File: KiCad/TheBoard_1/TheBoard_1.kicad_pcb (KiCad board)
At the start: 2 copper layers, 27 parts, among them J1 Conn_01x16_Female, J2 Conn_01x16_Female, U1 TL431D, U2 TL431D, U3 YAAJ_BlackPill_Part_Like_SWD_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, U4 TL431D, U5 TL431D

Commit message: progress
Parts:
- added J3: Conn_01x01_Male, Connector_PinHeader_2.54mm:PinHeader_1x01_P2.54mm_Vertical, F.Cu at (188.8, 80.0)
- added J4: Conn_01x01_Male, Connector_PinHeader_2.54mm:PinHeader_1x01_P2.54mm_Vertical, F.Cu at (188.2, 125.5)
- added J5: Conn_01x01_Male, Connector_PinHeader_2.54mm:PinHeader_1x01_P2.54mm_Vertical, F.Cu at (94.2, 145.8)
- added J6: Conn_01x01_Male, Connector_PinHeader_2.54mm:PinHeader_1x01_P2.54mm_Vertical, F.Cu at (102.0, 108.5)
- U3: value YAAJ_BlackPill_Part_Like_SWD_Breakout -> YAAJ_WeAct_BlackPill_Part_Like_SWD_Breakout
- moved U5 28.5 mm to (190.0, 97.4)
- moved Cref4 28.3 mm to (178.7, 144.5), turned to -90 degrees
- moved R3 28.0 mm to (182.3, 91.5)
- moved Cref3 26.6 mm to (180.2, 95.6), turned to -90 degrees
- moved R4 23.3 mm to (180.8, 139.0)
- moved U4 17.9 mm to (188.2, 146.3)
- moved R_SDA3 15.0 mm to (193.8, 66.3), turned to 180 degrees
- moved R_SCL3 13.3 mm to (193.8, 61.5), turned to 180 degrees
- moved R_SCL4 13.1 mm to (193.5, 107.3), turned to 180 degrees
- moved Udac4 10.5 mm to (188.2, 119.3)
- moved R_SDA4 9.63 mm to (193.5, 111.8), turned to 180 degrees
- moved Udac3 9.59 mm to (188.8, 73.3)
- moved U3 6.02 mm to (149.8, 81.2)
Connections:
- U3 pad 1: unconnected-(U3-Pad1) -> Net-(U3-Pad1)
- U3 pad 10: unconnected-(U3-Pad10) -> Net-(U3-Pad10)
- U3 pad 11: unconnected-(U3-Pad11) -> Net-(R_SCL2-Pad2)
- U3 pad 13: unconnected-(U3-Pad13) -> Net-(R_SDA2-Pad2)
- U3 pad 17: unconnected-(U3-Pad17) -> Net-(U3-Pad17)
- U3 pad 2: unconnected-(U3-Pad2) -> Net-(R_SCL1-Pad2)
- U3 pad 27: unconnected-(U3-Pad27) -> Net-(R_SDA1-Pad2)
- U3 pad 30: unconnected-(U3-Pad30) -> Net-(U3-Pad30)
- U3 pad 31: unconnected-(U3-Pad31) -> Net-(R_SCL4-Pad2)
- U3 pad 33: unconnected-(U3-Pad33) -> Net-(R_SDA4-Pad2)
- U3 pad 37: unconnected-(U3-Pad37) -> Net-(R_SCL3-Pad2)
- U3 pad 39: (no net) -> unconnected-(U3-Pad39)
- U3 pad 4: unconnected-(U3-Pad4) -> Net-(R_SDA3-Pad2)
- U3 pad 40: (no net) -> unconnected-(U3-Pad40)
- U3 pad 41: (no net) -> unconnected-(U3-Pad41)
- U3 pad 42: (no net) -> unconnected-(U3-Pad42)
- U3 pad 43: (no net) -> unconnected-(U3-Pad43)
- U3 pad 44: (no net) -> unconnected-(U3-Pad44)
- Udac1 pad 2: unconnected-(Udac1-Pad2) -> Net-(U3-Pad1)
- Udac2 pad 2: unconnected-(Udac2-Pad2) -> Net-(U3-Pad10)
- Udac3 pad 2: unconnected-(Udac3-Pad2) -> Net-(U3-Pad17)
- Udac4 pad 2: unconnected-(Udac4-Pad2) -> Net-(U3-Pad30)
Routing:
- net +2V5: track 5.72 -> 98.8 mm
- net +5V: track 0.00 -> 55.5 mm
- net GND: track 7.49 -> 52.6 mm
- net Net-(J2-Pad9): track 0.00 -> 30.4 mm
- net Net-(J2-Pad1): track 0.00 -> 29.8 mm
- net Net-(J2-Pad11): track 0.00 -> 26.3 mm
- net Net-(J2-Pad3): track 0.00 -> 26.1 mm
- net Net-(J2-Pad13): track 0.00 -> 22.5 mm
- net Net-(J2-Pad5): track 0.00 -> 22.2 mm
- net Net-(J2-Pad15): track 0.00 -> 19.3 mm
- net Net-(J2-Pad7): track 0.00 -> 18.1 mm
- net Net-(R_SCL4-Pad2): track 0.00 -> 13.9 mm
- net Net-(R_SCL3-Pad2): track 0.00 -> 12.8 mm
- net Net-(R_SDA3-Pad2): track 0.00 -> 10.2 mm
- net Net-(R_SDA4-Pad2): track 0.00 -> 10.2 mm

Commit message: progress
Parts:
- removed Cref1, Cref2, Cref4: 100n, Capacitor_THT:C_Disc_D5.0mm_W2.5mm_P2.50mm
- removed J3, J4, J6: Conn_01x01_Male, Connector_PinHeader_2.54mm:PinHeader_1x01_P2.54mm_Vertical
- removed R1, R2, R4: R, Resistor_THT:R_Axial_DIN0207_L6.3mm_D2.5mm_P10.16mm_Horizontal
- removed U1, U2, U5: TL431D, Package_SO:SOIC-8_3.9x4.9mm_P1.27mm
- added J13: Conn_01x01_Male, Connector_PinHeader_2.54mm:PinHeader_1x01_P2.54mm_Vertical, F.Cu at (99.5, 53.0)
- added J14: Conn_01x01_Male, Connector_PinHeader_2.54mm:PinHeader_1x01_P2.54mm_Vertical, F.Cu at (204.5, 141.5)
- added J8: Conn_01x01_Male, Connector_PinHeader_2.54mm:PinHeader_1x01_P2.54mm_Vertical, F.Cu at (198.5, 141.5)
- moved J5 92.8 mm to (93.5, 53.0)
- moved U4 89.4 mm to (160.5, 61.2)
- moved Udac1 56.3 mm to (108.2, 80.8), turned to 180 degrees
- moved R_SDA2 54.1 mm to (104.1, 127.3), turned to 0 degrees
- moved R_SCL2 49.6 mm to (104.2, 123.3), turned to 0 degrees
- moved R3 46.4 mm to (153.1, 55.5)
- moved Cref3 45.0 mm to (152.6, 60.0)
- moved R_SDA1 33.3 mm to (103.4, 88.8), turned to 0 degrees
- moved Udac2 29.4 mm to (109.0, 115.2), turned to 180 degrees
- moved R_SCL1 29.2 mm to (103.4, 92.8), turned to 0 degrees
- moved R_SDA4 16.3 mm to (206.1, 101.4)
- moved R_SCL3 15.8 mm to (205.8, 71.8)
- moved Udac4 14.2 mm to (200.8, 112.7)
- moved Udac3 13.6 mm to (201.0, 79.3)
- moved R_SCL4 12.6 mm to (206.0, 105.7)
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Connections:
- J1 pad 4: Net-(J1-Pad4) -> Net-(Udac1-Pad7)
- J1 pad 5: Net-(J1-Pad5) -> Net-(Udac1-Pad10)
- J1 pad 6: Net-(J1-Pad6) -> Net-(Udac1-Pad11)
- J1 pad 7: Net-(J1-Pad7) -> Net-(Udac1-Pad12)
- J1 pad 8: Net-(J1-Pad8) -> Net-(Udac1-Pad13)
- J2 pad 1: Net-(J2-Pad1) -> Net-(Udac3-Pad13)
- J2 pad 10: Net-(J2-Pad10) -> Net-(Udac4-Pad12)
- J2 pad 11: Net-(J2-Pad11) -> Net-(Udac4-Pad11)
- J2 pad 12: Net-(J2-Pad12) -> Net-(Udac4-Pad10)
- J2 pad 13: Net-(J2-Pad13) -> Net-(Udac4-Pad7)
- J2 pad 14: Net-(J2-Pad14) -> Net-(Udac4-Pad6)
- J2 pad 15: Net-(J2-Pad15) -> Net-(Udac4-Pad5)
- J2 pad 16: Net-(J2-Pad16) -> Net-(Udac4-Pad4)
- J2 pad 2: Net-(J2-Pad2) -> Net-(Udac3-Pad12)
- J2 pad 3: Net-(J2-Pad3) -> Net-(Udac3-Pad11)
- J2 pad 4: Net-(J2-Pad4) -> Net-(Udac3-Pad10)
- J2 pad 5: Net-(J2-Pad5) -> Net-(Udac3-Pad7)
- J2 pad 6: Net-(J2-Pad6) -> Net-(Udac3-Pad6)
- J2 pad 7: Net-(J2-Pad7) -> Net-(Udac3-Pad5)
- J2 pad 8: Net-(J2-Pad8) -> Net-(Udac3-Pad4)
- J2 pad 9: Net-(J2-Pad9) -> Net-(Udac4-Pad13)
- J5 pad 1: +2V5 -> +5V
- Udac1 pad 1: unconnected-(Udac1-Pad1) -> Net-(Udac1-Pad1)
- Udac1 pad 10: Net-(J1-Pad9) -> Net-(Udac1-Pad10)
- Udac1 pad 11: Net-(J1-Pad11) -> Net-(Udac1-Pad11)
- Udac1 pad 12: Net-(J1-Pad13) -> Net-(Udac1-Pad12)
- Udac1 pad 13: Net-(J1-Pad15) -> Net-(Udac1-Pad13)
- Udac1 pad 4: Net-(J1-Pad16) -> Net-(J1-Pad1)
- Udac1 pad 5: Net-(J1-Pad14) -> Net-(J1-Pad2)
- Udac1 pad 6: Net-(J1-Pad12) -> Net-(J1-Pad3)
- Udac1 pad 7: Net-(J1-Pad10) -> Net-(Udac1-Pad7)
- Udac2 pad 1: unconnected-(Udac2-Pad1) -> Net-(Udac1-Pad1)
- Udac2 pad 10: Net-(J1-Pad1) -> Net-(J1-Pad13)
- Udac2 pad 11: Net-(J1-Pad3) -> Net-(J1-Pad14)
- Udac2 pad 12: Net-(J1-Pad5) -> Net-(J1-Pad15)
- Udac2 pad 13: Net-(J1-Pad7) -> Net-(J1-Pad16)
- Udac2 pad 4: Net-(J1-Pad8) -> Net-(J1-Pad9)
- Udac2 pad 5: Net-(J1-Pad6) -> Net-(J1-Pad10)
- Udac2 pad 6: Net-(J1-Pad4) -> Net-(J1-Pad11)
- Udac2 pad 7: Net-(J1-Pad2) -> Net-(J1-Pad12)
- Udac3 pad 1: unconnected-(Udac3-Pad1) -> Net-(Udac1-Pad1)
- Udac3 pad 10: Net-(J2-Pad8) -> Net-(Udac3-Pad10)
- Udac3 pad 11: Net-(J2-Pad6) -> Net-(Udac3-Pad11)
- Udac3 pad 12: Net-(J2-Pad4) -> Net-(Udac3-Pad12)
- Udac3 pad 13: Net-(J2-Pad2) -> Net-(Udac3-Pad13)
- Udac3 pad 4: Net-(J2-Pad1) -> Net-(Udac3-Pad4)
- Udac3 pad 5: Net-(J2-Pad3) -> Net-(Udac3-Pad5)
- Udac3 pad 6: Net-(J2-Pad5) -> Net-(Udac3-Pad6)
- Udac3 pad 7: Net-(J2-Pad7) -> Net-(Udac3-Pad7)
- Udac4 pad 1: unconnected-(Udac4-Pad1) -> Net-(Udac1-Pad1)
- Udac4 pad 10: Net-(J2-Pad16) -> Net-(Udac4-Pad10)
- Udac4 pad 11: Net-(J2-Pad14) -> Net-(Udac4-Pad11)
- Udac4 pad 12: Net-(J2-Pad12) -> Net-(Udac4-Pad12)
- Udac4 pad 13: Net-(J2-Pad10) -> Net-(Udac4-Pad13)
- Udac4 pad 4: Net-(J2-Pad9) -> Net-(Udac4-Pad4)
- Udac4 pad 5: Net-(J2-Pad11) -> Net-(Udac4-Pad5)
- Udac4 pad 6: Net-(J2-Pad13) -> Net-(Udac4-Pad6)
- Udac4 pad 7: Net-(J2-Pad15) -> Net-(Udac4-Pad7)
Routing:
- net Net-(U3-Pad4): track 10.2 -> 77.3 mm
- net Net-(J1-Pad9): track 0.00 -> 61.6 mm
- net Net-(J1-Pad1): track 0.00 -> 60.2 mm
- net +5V: track 55.5 -> 113.5 mm, vias 0 -> 4
- net Net-(Udac4-Pad4): track 0.00 -> 56.1 mm
- net Net-(J1-Pad10): track 0.00 -> 55.3 mm
- net Net-(Udac3-Pad4): track 0.00 -> 53.1 mm
- net Net-(J1-Pad2): track 0.00 -> 52.9 mm
- net Net-(R_SCL1-Pad2): track 0.00 -> 52.6 mm
- net Net-(Udac4-Pad5): track 0.00 -> 50.4 mm
- net Net-(R_SDA2-Pad2): track 10.1 -> 58.5 mm
- net Net-(J1-Pad11): track 0.00 -> 48.3 mm
- net +2V5: track 98.8 -> 147.0 mm, vias 0 -> 5
- net Net-(Udac3-Pad5): track 0.00 -> 47.7 mm
- net Net-(R_SCL2-Pad2): track 5.90 -> 52.5 mm
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- added copper zone on B.Cu, net GND
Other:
- board outline added: 150 x 100 mm

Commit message: progress - almost done
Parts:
- added H1: MountingHole, MountingHole:MountingHole_3mm, F.Cu at (223.8, 141.5)
- added H2: MountingHole, MountingHole:MountingHole_3mm, F.Cu at (85.2, 141.5)
- added H3: MountingHole, MountingHole:MountingHole_3mm, F.Cu at (85.2, 53.0)
- added H4: MountingHole, MountingHole:MountingHole_3mm, F.Cu at (223.8, 53.0)
- moved J13 87.3 mm to (186.8, 54.0)
- moved J5 87.3 mm to (180.8, 54.0)
- moved U4 26.2 mm to (134.9, 56.0), turned to 90 degrees
- moved R3 24.2 mm to (129.0, 53.6), turned to -90 degrees
- moved Cref3 19.4 mm to (133.6, 63.9), turned to 0 degrees
- moved J14 9.50 mm to (214.0, 141.5)
- moved J8 9.50 mm to (208.0, 141.5)
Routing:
- net Net-(Udac1-Pad1): track 0.00 -> 209.2 mm, vias 0 -> 4
- net +2V5: track 147.0 -> 289.0 mm
- net Net-(R_SDA1-Pad2): track 10.8 -> 139.5 mm, vias 0 -> 2
- net +5V: track 113.5 -> 215.9 mm
- net Net-(U3-Pad17): track 0.00 -> 78.6 mm

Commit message: progress - done
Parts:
- added J3: Conn_01x03_Male, Connector_PinHeader_2.54mm:PinHeader_1x03_P2.54mm_Vertical, F.Cu at (168.5, 54.0)
- moved J13 10.3 mm to (197.0, 53.0)
- moved J5 10.3 mm to (191.0, 53.0)
- moved Cref3 9.64 mm to (124.3, 61.4), turned to -90 degrees
- moved U4 7.11 mm to (132.2, 62.6), turned to 0 degrees
- moved R3 6.38 mm to (134.6, 56.8), turned to 180 degrees
- moved J14 3.01 mm to (211.0, 141.8)
- moved J8 3.01 mm to (205.0, 141.8)
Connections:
- U3 pad 19: unconnected-(U3-Pad19) -> GND
- U3 pad 34: unconnected-(U3-Pad34) -> Net-(U3-Pad34)
- U3 pad 35: unconnected-(U3-Pad35) -> Net-(U3-Pad35)
- U3 pad 39: unconnected-(U3-Pad39) -> GND
- U3 pad 7: unconnected-(U3-Pad7) -> Net-(U3-Pad7)
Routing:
- net +5V: track 215.9 -> 314.9 mm
- net Net-(U3-Pad7): track 0.00 -> 46.7 mm
- net Net-(U3-Pad34): track 0.00 -> 40.6 mm
- net Net-(U3-Pad35): track 0.00 -> 37.0 mm
- net +2V5: track 289.0 -> 310.6 mm

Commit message: sync pin and power outputs
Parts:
- removed J13, J14, J8: Conn_01x01_Male, Connector_PinHeader_2.54mm:PinHeader_1x01_P2.54mm_Vertical
- added J6: Conn_01x03_Male, Connector_PinHeader_2.54mm:PinHeader_1x03_P2.54mm_Vertical, F.Cu at (101.8, 53.0)
- added J7: Conn_01x03_Male, Connector_PinHeader_2.54mm:PinHeader_1x03_P2.54mm_Vertical, F.Cu at (207.2, 141.5)
- J5: value Conn_01x01_Male -> Conn_01x03_Male; footprint Connector_PinHeader_2.54mm:PinHeader_1x01_P2.54mm_Vertical -> Connector_PinHeader_2.54mm:PinHeader_1x03_P2.54mm_Vertical
- moved J5 16.2 mm to (207.2, 53.0), turned to 90 degrees
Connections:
- U3 pad 36: unconnected-(U3-Pad36) -> Net-(Udac1-Pad1)
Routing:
- net +2V5: track 310.6 -> 392.1 mm, vias 5 -> 6
- net +5V: track 314.9 -> 367.8 mm
- net Net-(Udac1-Pad1): track 209.2 -> 246.4 mm

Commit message: Change in spi
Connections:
- J3 pad 2: Net-(J3-Pad2) -> Net-(U3-Pad17)
- R_SCL3 pad 2: Net-(R_SCL3-Pad2) -> Net-(U3-Pad34)
- R_SDA3 pad 2: Net-(R_SDA3-Pad2) -> Net-(U3-Pad7)
- U3 pad 34: Net-(J3-Pad3) -> Net-(U3-Pad34)
- U3 pad 35: Net-(J3-Pad2) -> Net-(U3-Pad35)
- U3 pad 37: Net-(R_SCL3-Pad2) -> Net-(J3-Pad3)
- U3 pad 4: Net-(R_SDA3-Pad2) -> Net-(J3-Pad1)
- U3 pad 7: Net-(J3-Pad1) -> Net-(U3-Pad7)
- Udac3 pad 15: Net-(R_SDA3-Pad2) -> Net-(U3-Pad7)
- Udac3 pad 16: Net-(R_SCL3-Pad2) -> Net-(U3-Pad34)
- Udac3 pad 2: Net-(U3-Pad17) -> Net-(U3-Pad35)
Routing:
- net Net-(U3-Pad7): track 0.00 -> 83.6 mm
- net Net-(R_SDA3-Pad2): track 77.3 -> 0.00 mm
- net Net-(U3-Pad34): track 0.00 -> 69.0 mm
- net Net-(R_SCL3-Pad2): track 59.2 -> 0.00 mm
- net Net-(U3-Pad35): track 0.00 -> 40.4 mm
- net Net-(J3-Pad2): track 37.0 -> 0.00 mm
- net +5V: track 367.8 -> 398.8 mm, vias 4 -> 3
- net Net-(J3-Pad3): track 40.6 -> 35.0 mm
- net Net-(J3-Pad1): track 46.7 -> 41.2 mm
- net Net-(U3-Pad17): track 78.6 -> 74.7 mm
- net Net-(R_SDA1-Pad2): track 139.5 -> 138.0 mm, vias 2 -> 1

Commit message: QOL
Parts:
- added J4: Conn_01x02_Male, Connector_PinHeader_2.54mm:PinHeader_1x02_P2.54mm_Vertical, F.Cu at (177.5, 112.7)
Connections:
- U3 pad 40: unconnected-(U3-Pad40) -> Net-(J4-Pad2)
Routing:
- net Net-(J4-Pad2): track 0.00 -> 51.8 mm
- net +5V: track 398.8 -> 409.8 mm
- net Net-(J3-Pad3): track 35.0 -> 40.3 mm
- net Net-(J3-Pad2): track 74.7 -> 76.2 mm

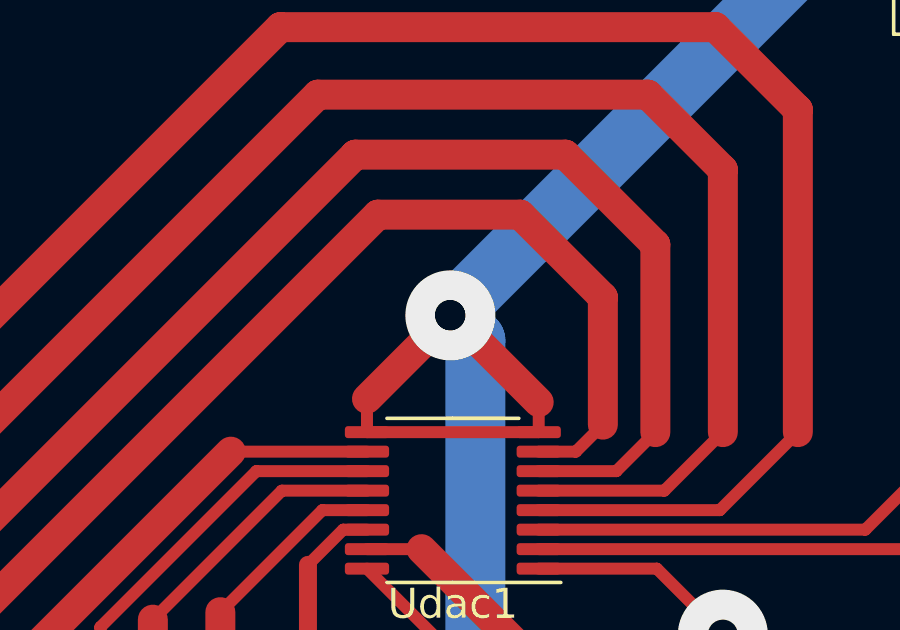
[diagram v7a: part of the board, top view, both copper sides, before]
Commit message: Fixind DRC checker error
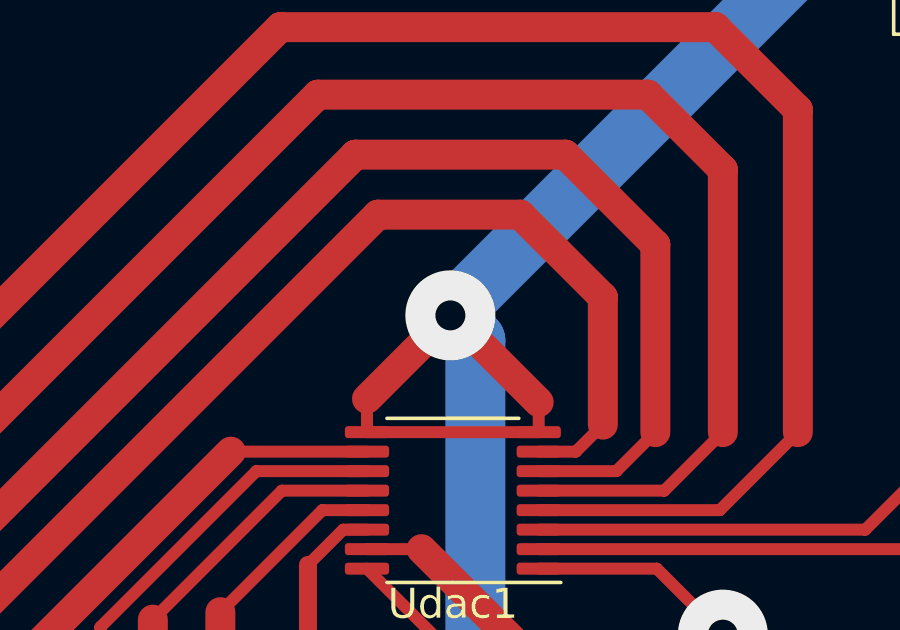
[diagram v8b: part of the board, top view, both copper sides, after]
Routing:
- net +2V5: vias 6 -> 5
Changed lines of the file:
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@@
   (via (at 109 108) (size 3) (drill 1) (layers "F.Cu" "B.Cu") (net 1))
   (via (at 201 85.265) (size 3) (drill 1) (layers "F.Cu" "B.Cu") (net 1))
-  (via (at 108.155 74.595) (size 2) (drill 1) (layers "F.Cu" "B.Cu") (net 1))
   (via (at 200.83 119.14) (size 3) (drill 1) (layers "F.Cu" "B.Cu") (net 1))
   (segment (start 108.155 74.595) (end 121.385 61.365) (width 2) (layer "B.Cu") (net 1))
